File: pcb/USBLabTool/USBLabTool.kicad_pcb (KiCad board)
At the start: 4 copper layers, 236 parts, among them J1 Conn_01x06_Pin, J17 2x01, J19 T_N5V, J2 Conn_02x12_Odd_Even, J20 USB_C_Receptacle, K1 G5V-2, K2 G5V-2, Q1 STL11N3LLH6, SW1 TS02-66-73-BK-100-SCR-D, U1 AQY284SX, U10 MC33274ADR2G, U11 DG403, U12 STM32H562VGTx, U13 R1283K002A, U14 ST1L05APU33R, U15 ST1L05APU33R, U16 LTC1983ES6-5TRMPBF, U17 TCPP01-M12, U18 74HC245, U19 USBLC6-2SC6, U2 AQY284SX, U20 74HC245, U3 CD74HC4316, U4 LMP7718, U5 CD74HC4316, U6 LMP7718, U7 OPA863, U8 OPA863, U9 MC33274ADR2G, Y1 32.768kHz, Y2 NX2016SA-25M-EXS00A-CS08742

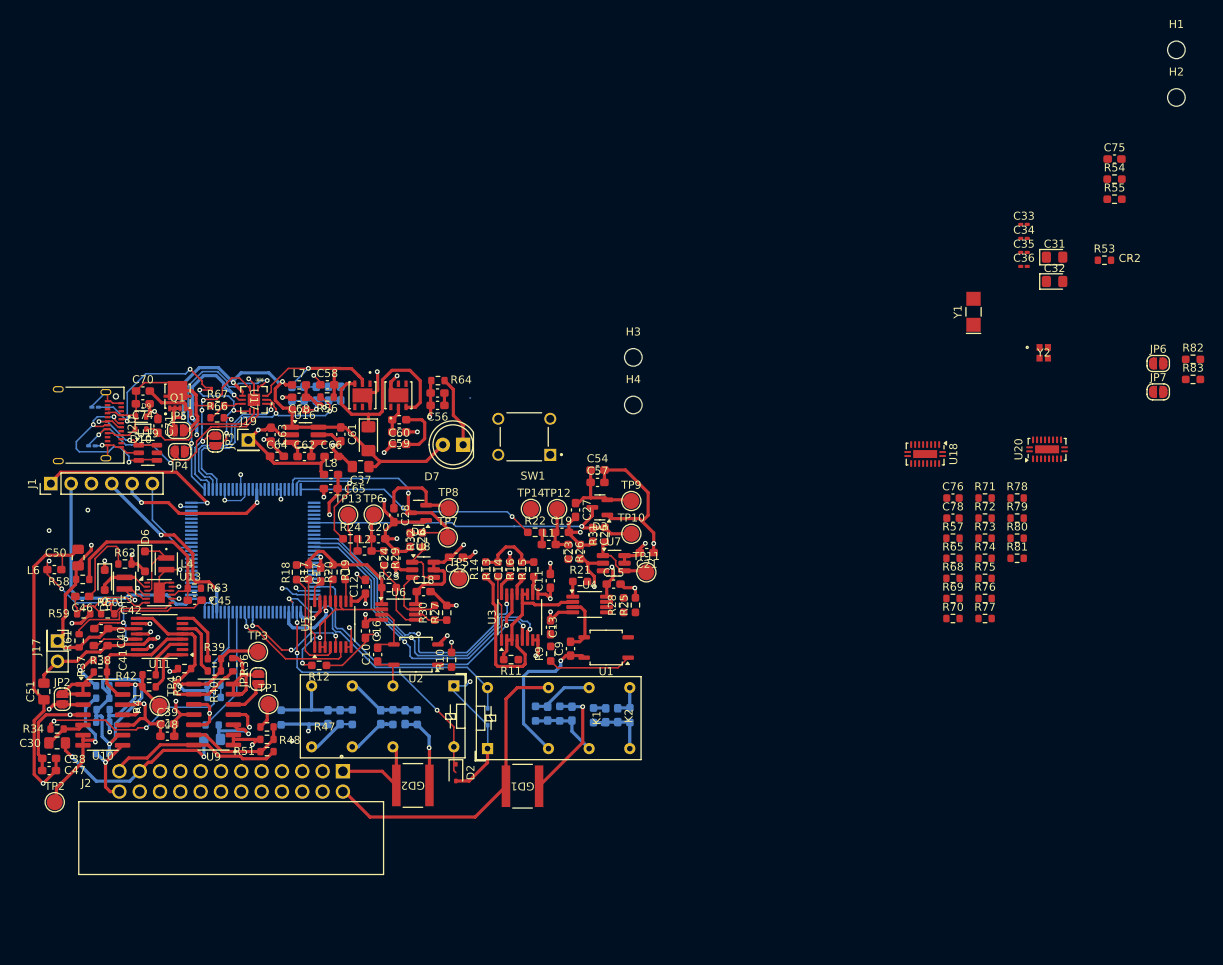
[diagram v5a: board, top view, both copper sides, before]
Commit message: nearly finish MCU, need checking, and unfinished logic analyzer
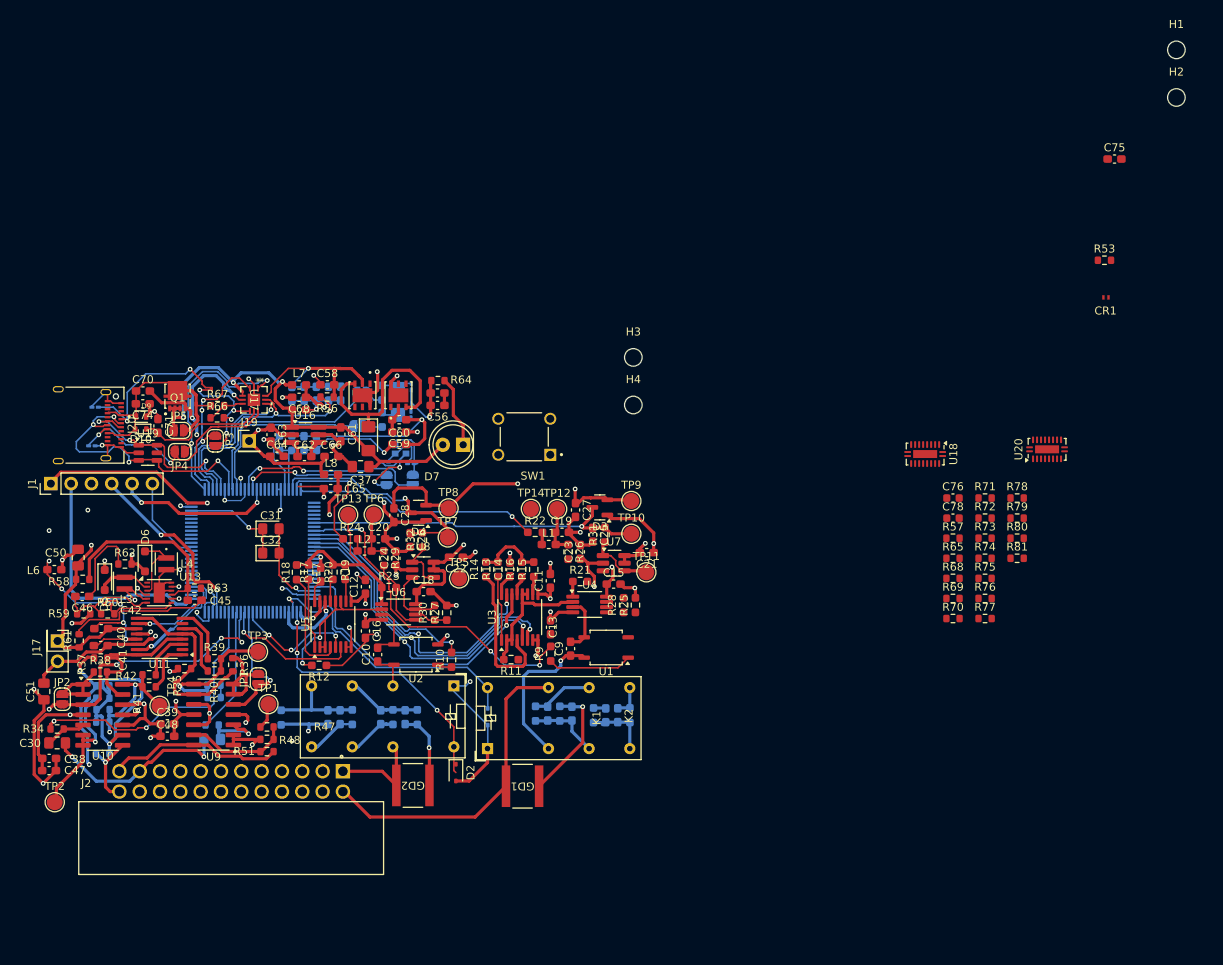
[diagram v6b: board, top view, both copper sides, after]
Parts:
- removed CR2: ESDALC6V1-1U2, userfp:DIODE_ESDALC6V1-1U2_STM
- added CR1: ESDALC6V1-1M2, userfp:SOD882_STM, F.Cu at (189.9, 78.7)
- added JP8: SJ, Jumper:SolderJumper-2_P1.3mm_Open_RoundedPad1.0x1.5mm, B.Cu at (96.8, 90.6)
- added JP9: SJ, Jumper:SolderJumper-2_P1.3mm_Open_RoundedPad1.0x1.5mm, B.Cu at (96.5, 94.8)
- C33, C34, C35, C36, C54, C57, JP6, JP7, R54, R55, R82, R83, Y1, Y2: moved to B.Cu
- moved R55 108.7 mm to (86.6, 96.9), turned to -90 degrees
- moved R54 108.0 mm to (88.1, 96.9), turned to -90 degrees
- moved C31 103.7 mm to (85.5, 107.6)
- moved C32 103.7 mm to (85.5, 110.6)
- moved R83 101.5 mm to (99.4, 94.0), turned to -90 degrees
- moved R82 101.5 mm to (99.4, 90.6), turned to -90 degrees
- moved JP7 97.1 mm to (100.0, 101.5), turned to 90 degrees
- moved JP6 94.3 mm to (103.2, 101.5), turned to 90 degrees
- moved C34 84.6 mm to (99.8, 99.2), turned to 180 degrees
- moved C33 82.3 mm to (103.0, 99.5), turned to 180 degrees
- moved Y2 81.3 mm to (101.7, 97.7), turned to -90 degrees
- moved C36 78.8 mm to (103.0, 93.3), turned to -90 degrees
- moved C35 78.4 mm to (103.0, 89.8), turned to 90 degrees
- moved Y1 72.8 mm to (101.4, 91.7)
- moved C54 36.8 mm to (89.6, 96.9), turned to -90 degrees
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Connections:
- R82 pad 2: RCC_OSC32_IN -> Net-(JP8-B)
- R83 pad 2: RCC_OSC32_OUT -> Net-(JP9-B)
- U12 pad 18: CH0_ACDC -> unconnected-(U12-PC3-Pad18)
- U12 pad 26: GAIN_C0 -> unconnected-(U12-PA3-Pad26)
- U12 pad 29: C0_IN -> unconnected-(U12-PA4-Pad29)
- U12 pad 30: C1_IN -> unconnected-(U12-PA5-Pad30)
- U12 pad 32: GAIN_C1 -> unconnected-(U12-PA7-Pad32)
- U12 pad 34: unconnected-(U12-PC5-Pad34) -> CH0_ACDC
- U12 pad 5: unconnected-(U12-PE6-Pad5) -> USB_D-
- U12 pad 64: unconnected-(U12-PC7-Pad64) -> C0_IN
- U12 pad 66: unconnected-(U12-PC9-Pad66) -> C1_IN
- U12 pad 7: unconnected-(U12-PC13-Pad7) -> USB_D+
- U12 pad 70: USB_FN_N -> unconnected-(U12-PA11-Pad70)
- U12 pad 71: USB_FN_P -> unconnected-(U12-PA12-Pad71)
- U12 pad 78: unconnected-(U12-PC10-Pad78) -> GAIN_C0
- U12 pad 79: unconnected-(U12-PC11-Pad79) -> GAIN_C1
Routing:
- net CH1_ACDC: track 0.00 -> 41.9 mm, vias 0 -> 3
- net -5VCLEAN: track 81.1 -> 121.9 mm, vias 11 -> 12
- net C1_IN: track 4.49 -> 34.5 mm, vias 1 -> 4
- net GND: track 220.7 -> 248.1 mm, vias 27 -> 28
- net +3.3VA: track 29.1 -> 54.4 mm, vias 0 -> 3
- net RCC_OSC32_IN: track 0.00 -> 25.2 mm
- net CH0_ACDC: track 1.32 -> 26.5 mm
- net RCC_OSC_IN: track 0.00 -> 24.5 mm, vias 0 -> 2
- net RCC_OSC32_OUT: track 0.00 -> 22.3 mm
- net RCC_OSC_OUT: track 0.00 -> 18.7 mm, vias 0 -> 2
- net GNDA: track 233.6 -> 219.1 mm, vias 23 -> 26
- net USB_D-: track 11.9 -> 25.6 mm, vias 2 -> 3
- net USB_D+: track 22.3 -> 35.5 mm, vias 3 -> 4
- net Net-(C31-Pad1): track 0.00 -> 12.9 mm, vias 0 -> 1
- net GAIN_C1: track 2.00 -> 14.7 mm
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- added copper zone on In2.Cu, net +3.3VA

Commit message: try to do logic analyzer
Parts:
- C76, C78, R57, R65, R68, R69, R70, R71, R72, R73, R74, R75, R76, R77, R78, R79, R80, R81, U18, U20: moved to B.Cu
- U12: value STM32H562VGTx -> STM32H563VITx
- moved R81 109.7 mm to (71.7, 135.0), turned to 90 degrees
- moved R73 108.7 mm to (71.6, 143.1), turned to 90 degrees
- moved R79 108.5 mm to (74.2, 135.0), turned to 90 degrees
- moved R71 107.9 mm to (74.2, 143.1), turned to 90 degrees
- moved U20 106.4 mm to (89.1, 148.5), turned to -90 degrees
- moved U18 103.0 mm to (76.7, 147.1), turned to 90 degrees
- moved R80 100.4 mm to (81.8, 134.9), turned to -90 degrees
- moved R72 100.0 mm to (81.8, 143.1), turned to -90 degrees
- moved R77 99.8 mm to (76.3, 135.0), turned to 90 degrees
- moved R78 99.5 mm to (84.3, 134.9), turned to -90 degrees
- moved C76 99.4 mm to (81.0, 146.6), turned to 90 degrees
- moved R75 97.8 mm to (79.2, 134.9), turned to 90 degrees
- moved R69 97.8 mm to (76.7, 143.1), turned to 90 degrees
- moved R65 96.8 mm to (79.3, 143.1), turned to 90 degrees
- moved C78 96.5 mm to (84.7, 149.8)
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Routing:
- net GND: track 248.1 -> 336.7 mm, vias 28 -> 42
- net +3.3V: track 73.6 -> 138.1 mm, vias 5 -> 11
- net LOGIC_INP0: track 0.00 -> 32.4 mm, vias 0 -> 1
- net NRST: track 30.4 -> 61.9 mm, vias 2 -> 4
- net LOGIC_INP1: track 0.00 -> 22.7 mm, vias 0 -> 1
- net LOGIC_INP2: track 0.00 -> 20.6 mm, vias 0 -> 1
- net LOGIC_INP3: track 0.00 -> 18.7 mm, vias 0 -> 1
- net LOGIC_INP13: track 0.00 -> 18.3 mm, vias 0 -> 2
- net LOGIC_INP4: track 0.00 -> 17.2 mm, vias 0 -> 1
- net LOGIC_INP10: track 0.00 -> 16.4 mm, vias 0 -> 2
- net Net-(U9D--): track 14.6 -> 30.9 mm, vias 0 -> 1
- net LOGIC_INP15: track 0.00 -> 16.2 mm
- net LOGIC_INP14: track 0.00 -> 16.0 mm, vias 0 -> 2
- net LOGIC_INP5: track 0.00 -> 15.9 mm, vias 0 -> 1
- net LOGIC_INP11: track 0.00 -> 15.3 mm, vias 0 -> 2
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
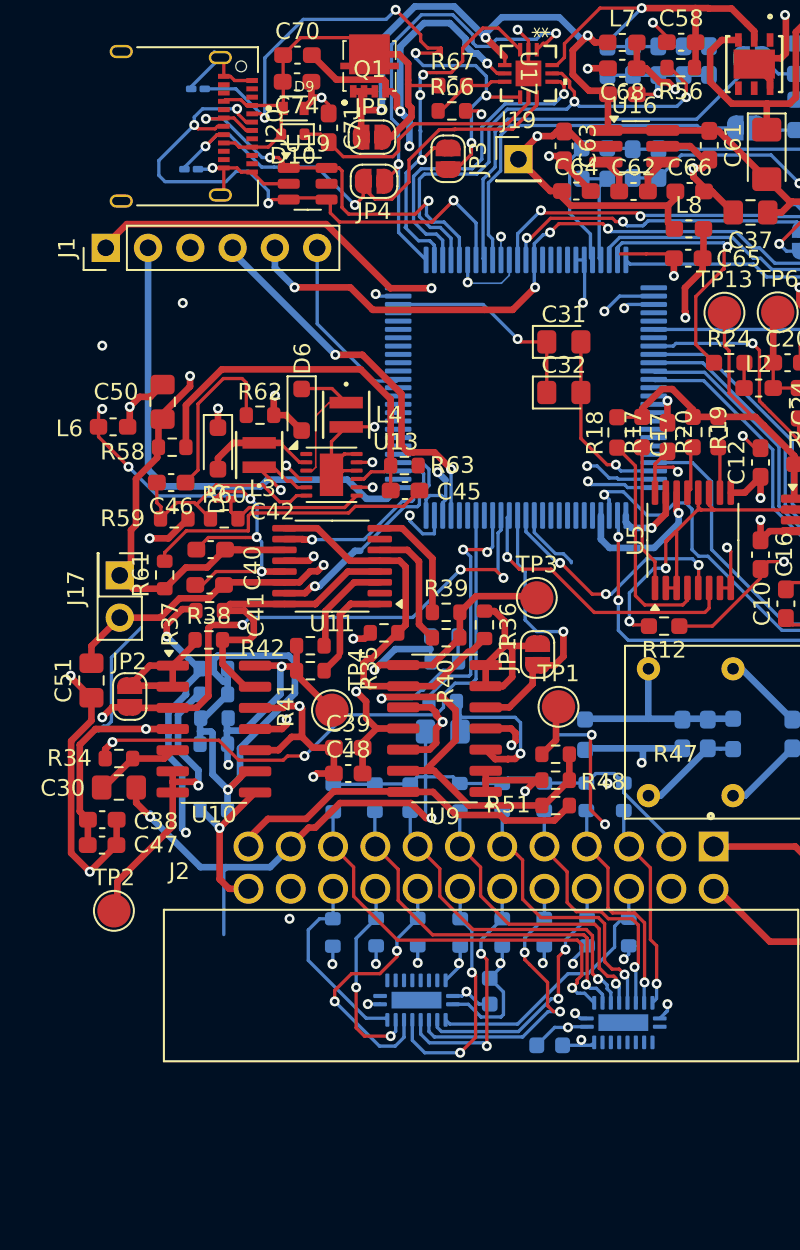
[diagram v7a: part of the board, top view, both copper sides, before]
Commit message: clean up layout and create space for logic analyzer
check discord for new MCU pins
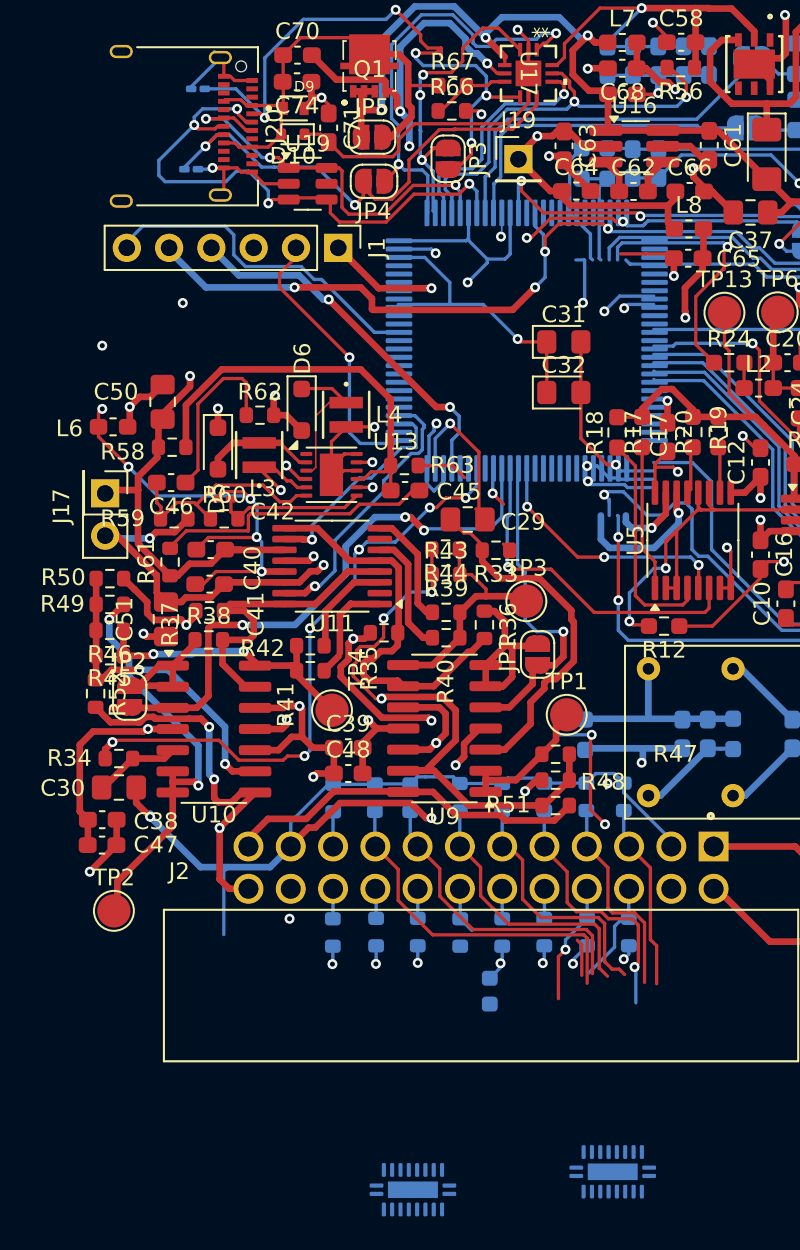
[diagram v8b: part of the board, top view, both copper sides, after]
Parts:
- removed C78: 100nF, Capacitor_SMD:C_0603_1608Metric
- C29, R33, R43, R44, R45, R46, R49, R50, R52: moved to F.Cu
- moved J1 14.0 mm to (72.0, 102.0), turned to -90 degrees
- moved C29 12.8 mm to (79.7, 118.3), turned to 0 degrees
- moved U18 11.4 mm to (76.4, 158.5)
- moved R52 9.95 mm to (57.4, 128.7), turned to -90 degrees
- moved R33 9.64 mm to (81.4, 120.1), turned to 180 degrees
- moved R46 9.26 mm to (58.2, 124.9)
- moved U20 8.99 mm to (88.4, 157.4)
- moved R49 8.26 mm to (58.2, 123.4), turned to 180 degrees
- moved R50 8.26 mm to (58.2, 121.8), turned to 0 degrees
- moved R45 7.32 mm to (58.2, 126.5)
- moved C51 5.79 mm to (61.6, 124.3)
- moved R43 5.24 mm to (78.4, 121.6), turned to 0 degrees
- moved R44 5.24 mm to (78.4, 120.0), turned to 180 degrees
- moved J17 5.00 mm to (58.0, 116.7)
- moved U12 2.83 mm to (83.3, 107.5)
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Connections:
- U12 pad 24: TIM2_CH2 -> ADC2_INP3
- U12 pad 25: TIM2_CH3 -> TIM2_CH2
- U12 pad 26: unconnected-(U12-PA3-Pad26) -> TIM2_CH3
- U12 pad 31: ADC2_INP3 -> unconnected-(U12-PA6-Pad31)
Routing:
- net +3.3V: track 138.1 -> 103.3 mm, vias 11 -> 9
- net LOGIC_INP0: track 32.4 -> 4.31 mm, vias 1 -> 0
- net -5VCLEAN: track 122.1 -> 105.5 mm
- net LOGIC_INP13: track 18.3 -> 1.78 mm, vias 2 -> 0
- net LOGIC_INP10: track 16.4 -> 1.78 mm, vias 2 -> 0
- net GND: track 336.7 -> 322.4 mm, vias 42 -> 37
- net LOGIC_INP12: track 15.2 -> 1.80 mm, vias 2 -> 0
- net DAC1_OUT2: track 9.71 -> 23.0 mm, vias 1 -> 3
- net DEBUG_JTCK_SWCLK: track 29.7 -> 16.7 mm, vias 0 -> 1
- net LOGIC_INP11: track 15.3 -> 2.80 mm, vias 2 -> 0
- net TIM1_CH1: track 14.8 -> 3.05 mm, vias 2 -> 1
- net Net-(U9A-+): track 10.0 -> 21.7 mm, vias 1 -> 0
- net LOGIC_INP9: track 12.2 -> 1.79 mm, vias 2 -> 0
- net LOGIC_INP15: track 16.2 -> 6.34 mm
- net LOGIC_INP8: track 11.6 -> 1.81 mm
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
